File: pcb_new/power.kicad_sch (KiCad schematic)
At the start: 36 parts, among them J3 SACC-DSIV-M12MS-5CON-L180, J7 USB4105-GF-A, U11 TPS2023DR, U12 LM1085ISX-3.3/NOPB, U13 INA226AIDGSR

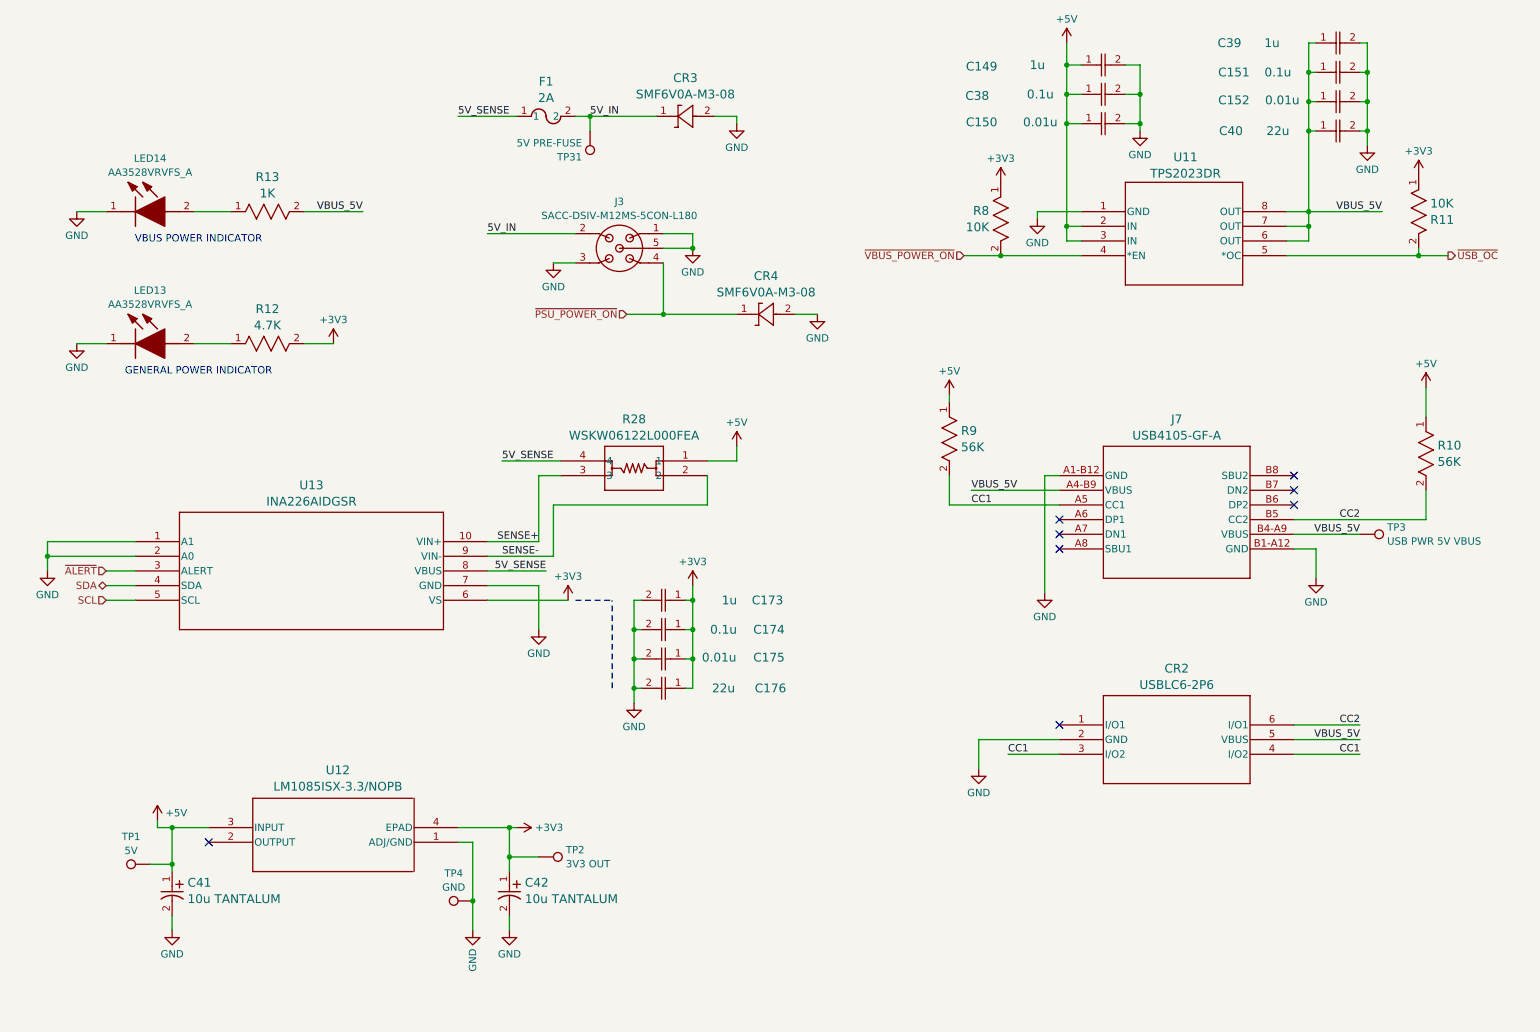
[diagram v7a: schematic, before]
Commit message: mux USB rails (ref #96), adjust CC resistors (ref #87)
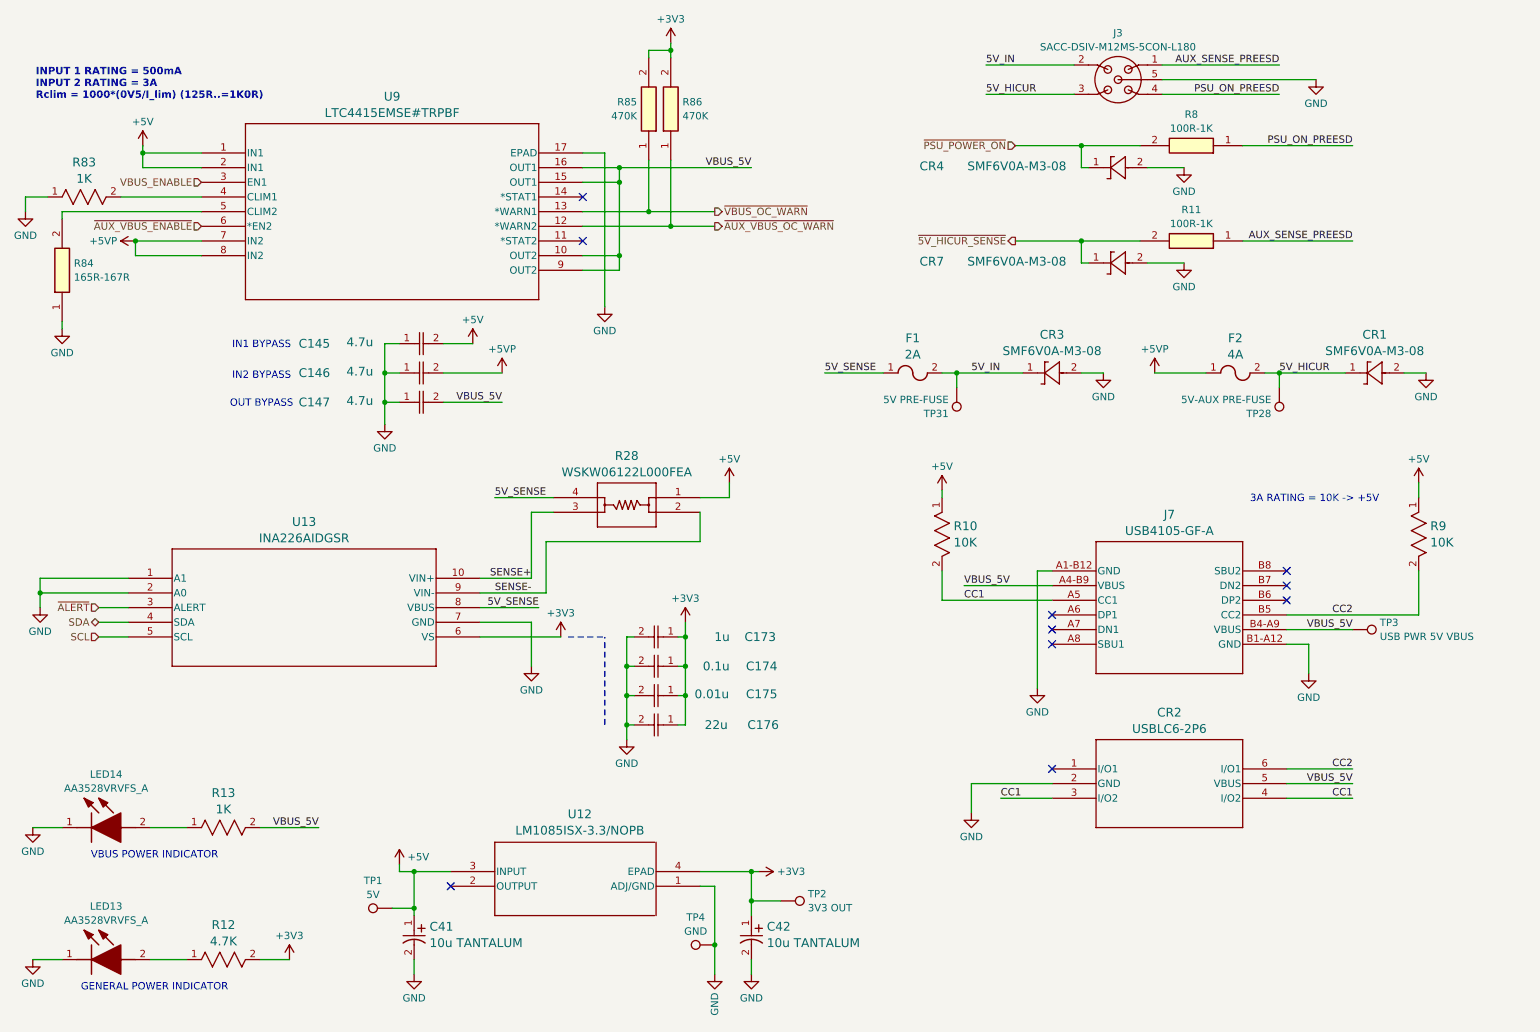
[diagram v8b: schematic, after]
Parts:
- removed C149, C39: 1u, OroLink:cap_UMK105 CG080CV-F_TAY, symbol OroLink:JMK105BJ105KVHF
- removed C150, C152: 0.01u, OroLink:CAP_0402_N_WAL, symbol OroLink:0402B103J160CT
- removed C151, C38: 0.1u, OroLink:CAP_MSAS1L-3_TAY, symbol OroLink:MSAST1L3YB5104KFNA01
- removed C40: 22u, OroLink:CAP_CL10_SAM, symbol OroLink:CL10A226MO7JZNC
- removed R10, R9: 56K, OroLink:RC0603N_PAN, symbol OroLink:ERJ-3GEYJ563V
- removed R11, R8: 10K, OroLink:STA_RMCF0402_STP, symbol OroLink:RMCF0402FT10K0
- removed U11: TPS2023DR, OroLink:D8, symbol OroLink:TPS2023DR
- added C145, C146, C147: 4.7u, OroLink:GRM15x, symbol OroLink:GRM155C61E475ME15J
- added CR1, CR7: SMF6V0A-M3-08, OroLink:ZDO_SMF_DO-219AB_VIS, symbol OroLink:SMF6V0A-M3-08
- added F2: 4A, OroLink:0697_BEL, symbol OroLink:0697H4000-01
- added R10, R9: 10K, OroLink:STA_RMCF0402_STP, symbol OroLink:RMCF0402FT10K0
- added R11, R8: 100R-1K, OroLink:RESC1005X40N, symbol OroLink:CR0402-FX-1650GLF
- added R83: 1K, OroLink:RES_SG73P_2A_KOA, symbol OroLink:SG73P2ATTD102J
- added R84: 165R-167R, OroLink:RESC1005X40N, symbol OroLink:CR0402-FX-1650GLF
- added R85, R86: 470K, OroLink:CRCW0402470KFKED, symbol OroLink:CRCW0402470KFKED
- added TP28: 5V-AUX PRE-FUSE, TestPoint:TestPoint_Pad_1.0x1.0mm, symbol Connector:TestPoint
- added U9: LTC4415EMSE#TRPBF, OroLink:MSOP-16_MSE_LIT, symbol OroLink:LTC4415EMSE-TRPBF
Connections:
- net +3V3: now also R85.2, R86.2
- net +5V: now also C145.2, R10.1, R9.1, U9.1 (IN1), U9.2 (IN1)
- net CC1: now also R10.2
- net CC2: now also R9.2
- net GND: now also C145.1, C146.1, C147.1, CR1.2, CR7.2, R83.1, R84.1, U9.17 (EPAD); no longer J3.1, J3.3
- net VBUS_5V: now also C147.2, U9.10 (OUT2), U9.15 (OUT1), U9.16 (OUT1), U9.9 (OUT2)
- net ~{PSU_POWER_ON}: now also R8.2; no longer J3.4
- new net: R84.2, U9.5 (CLIM2)
- new net: R83.2, U9.4 (CLIM1)
- new net +5VP: C146.2, F2.1, U9.7 (IN2), U9.8 (IN2)
- new net 5V_HICUR: CR1.1, F2.2, J3.3, TP28.1
- new net AUX_SENSE_PREESD: J3.1, R11.1
- new net PSU_ON_PREESD: J3.4, R8.1
- new net VBUS_ENABLE: U9.3 (EN1)
- new net ~{5V_HICUR_SENSE}: CR7.1, R11.2
- new net ~{AUX_VBUS_ENABLE}: U9.6 (*EN2)
- new net ~{AUX_VBUS_OC_WARN}: R86.1, U9.12 (*WARN2)
- new net ~{VBUS_OC_WARN}: R85.1, U9.13 (*WARN1)
- no-connect marks 8 -> 10
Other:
- note added: "3A RATING = 10K -> +5V"
- note added: "IN1 BYPASS"
- note added: "IN2 BYPASS"
- note added: "INPUT 1 RATING = 500mA INPUT 2 RATING = 3A Rclim = 1000*(0V5/I_lim) (125R..=1K0R)"
- note added: "OUT BYPASS"
- moved on the sheet: C173, C174, C175, C176, C41, C42, CR2, CR3, CR4, J3, J7, LED13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
